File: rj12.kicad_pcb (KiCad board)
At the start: 2 copper layers, 16.3 x 21 mm, 2 parts, among them J1 Conn_01x06, P1 RJ12_Housing

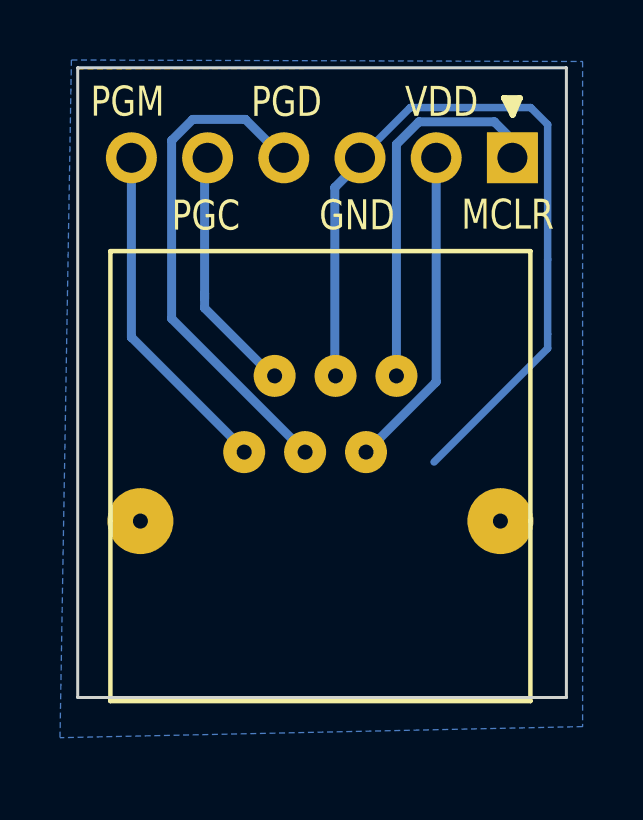
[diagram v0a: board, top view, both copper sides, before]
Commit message: Change the outline more compact
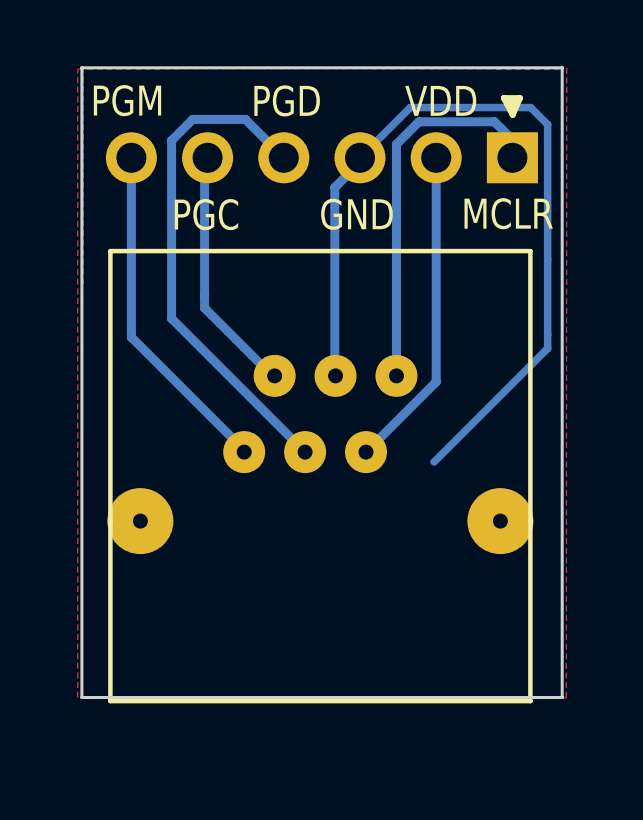
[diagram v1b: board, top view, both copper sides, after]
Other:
- board size 16.3 x 21 mm -> 16 x 21 mm
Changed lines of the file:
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@@
     (links 6)
     (no_connects 0)
-    (area 159.349999 99.449999 175.740001 120.540001)
+    (area 149.500001 95.849945 177.295 121.830001)
     (thickness 1.6)
-    (drawings 31)
+    (drawings 33)
     (tracks 34)
     (zones 0)
@@
     )
   )
+  (dimension 20.98 (width 0.3) (layer Eco1.User)
+    (gr_text "20.980 mm" (at 156 110 270) (layer Eco1.User)
+      (effects (font (size 1.5 1.5) (thickness 0.3)))
+    )
+    (feature1 (pts (xy 159.4 120.49) (xy 154.65 120.49)))
+    (feature2 (pts (xy 159.4 99.51) (xy 154.65 99.51)))
+    (crossbar (pts (xy 157.35 99.51) (xy 157.35 120.49)))
+    (arrow1a (pts (xy 157.35 120.49) (xy 156.763579 119.363496)))
+    (arrow1b (pts (xy 157.35 120.49) (xy 157.936421 119.363496)))
+    (arrow2a (pts (xy 157.35 99.51) (xy 156.763579 100.636504)))
+    (arrow2b (pts (xy 157.35 99.51) (xy 157.936421 100.636504)))
+  )
+  (dimension 16.000012 (width 0.3) (layer Eco1.User)
+    (gr_text "16.000 mm" (at 167.552825 97.239954 359.9283803) (layer Eco1.User)
+      (effects (font (size 1.5 1.5) (thickness 0.3)))
+    )
+    (feature1 (pts (xy 175.55 99.51) (xy 175.554513 95.899955)))
+    (feature2 (pts (xy 159.55 99.49) (xy 159.554513 95.879955)))
+    (crossbar (pts (xy 159.551138 98.579953) (xy 175.551138 98.599953)))
+    (arrow1a (pts (xy 175.551138 98.599953) (xy 174.423902 99.184965)))
+    (arrow1b (pts (xy 175.551138 98.599953) (xy 174.425368 98.012125)))
+    (arrow2a (pts (xy 159.551138 98.579953) (xy 160.676908 99.167781)))
+    (arrow2b (pts (xy 159.551138 98.579953) (xy 160.678374 97.994941)))
+  )
   (gr_line (start 174.14 100.51) (end 173.9 101.07) (layer F.SilkS) (width 0.2))
   (gr_line (start 173.61 100.51) (end 174.14 100.51) (layer F.SilkS) (width 0.2))
-  (gr_line (start 175.69 99.5) (end 175.69 120.49) (layer Edge.Cuts) (width 0.1))
+  (gr_line (start 175.55 99.5) (end 175.55 120.49) (layer Edge.Cuts) (width 0.1))
   (gr_line (start 166.59 116.81) (end 165.91 117.33) (layer B.SilkS) (width 0.2))
   (gr_line (start 166.41 116.54) (end 165.65 116.64) (layer B.SilkS) (width 0.2))
@@
     (effects (font (size 1 1) (thickness 0.25)) (justify mirror))
   )
-  (gr_line (start 159.4 99.5) (end 159.4 120.49) (layer Edge.Cuts) (width 0.1))
-  (gr_line (start 159.4 99.5) (end 175.69 99.5) (layer Edge.Cuts) (width 0.1))
-  (gr_line (start 159.4 120.49) (end 175.69 120.49) (layer Edge.Cuts) (width 0.1))
+  (gr_line (start 159.54 99.5) (end 159.54 120.49) (layer Edge.Cuts) (width 0.1))
+  (gr_line (start 159.54 99.5) (end 175.55 99.5) (layer Edge.Cuts) (width 0.1))
+  (gr_line (start 159.54 120.49) (end 175.55 120.49) (layer Edge.Cuts) (width 0.1))
   (gr_text PGM (at 161.06 100.63) (layer F.SilkS)
     (effects (font (size 1 0.8) (thickness 0.2)))
@@
   (segment (start 171.35 109.97) (end 169.01 112.31) (width 0.3) (layer B.Cu) (net 2))
   (segment (start 171.5 102.5) (end 171.3 102.7) (width 0.3) (layer B.Cu) (net 2))
+  (segment (start 175.065001 105.884999) (end 175.065001 108.374999) (width 0.25) (layer B.Cu) (net 3))
   (segment (start 175.065001 108.854999) (end 171.28 112.64) (width 0.25) (layer B.Cu) (net 3))
   (segment (start 175.065001 108.374999) (end 175.065001 108.854999) (width 0.25) (layer B.Cu) (net 3))
-  (segment (start 175.065001 105.884999) (end 175.065001 108.374999) (width 0.25) (layer B.Cu) (net 3))
+  (segment (start 175.065001 101.389999) (end 175.065001 105.884999) (width 0.25) (layer B.Cu) (net 3))
+  (segment (start 174.499991 100.824989) (end 175.065001 101.389999) (width 0.25) (layer B.Cu) (net 3))
   (segment (start 168.81 102.5) (end 170.485011 100.824989) (width 0.25) (layer B.Cu) (net 3))
   (segment (start 170.485011 100.824989) (end 174.499991 100.824989) (width 0.25) (layer B.Cu) (net 3))
-  (segment (start 174.499991 100.824989) (end 175.065001 101.389999) (width 0.25) (layer B.Cu) (net 3))
-  (segment (start 175.065001 101.389999) (end 175.065001 105.884999) (width 0.25) (layer B.Cu) (net 3))
   (segment (start 168.96 102.5) (end 167.970005 103.489995) (width 0.3) (layer B.Cu) (net 3))
   (segment (start 167.970005 103.489995) (end 167.970005 109.745005) (width 0.3) (layer B.Cu) (net 3))
@@
     (polygon
       (pts
-        (xy 159.19 99.24) (xy 176.23 99.29) (xy 176.23 121.46) (xy 158.81 121.83)
+        (xy 159.58 99.51) (xy 175.53 99.54) (xy 175.55 120.47) (xy 159.54 120.47)
       )
     )

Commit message: Added a txt V.01 to indicate version 1 and added gerber file to be panelized
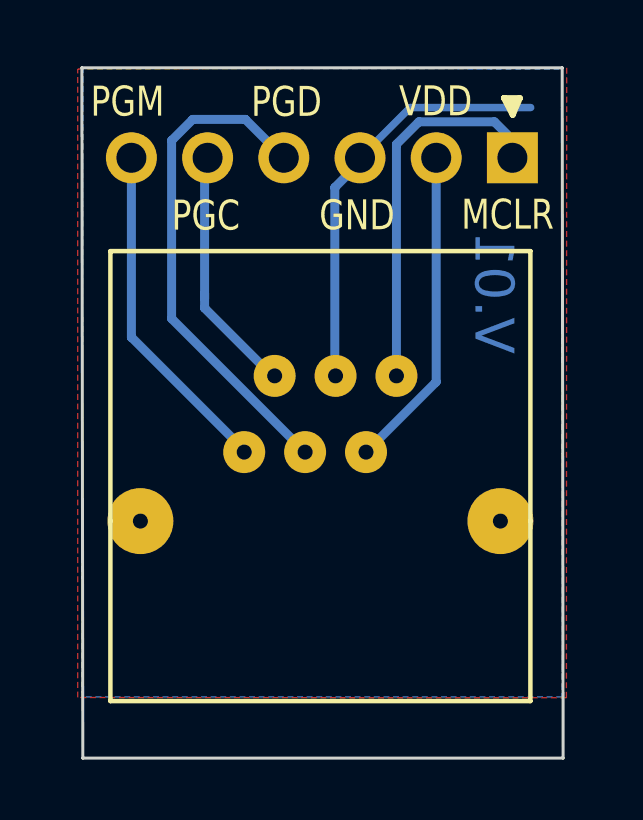
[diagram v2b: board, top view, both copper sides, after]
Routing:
- net pin3: track 27.8 -> 14.1 mm
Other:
- board size 16 x 21 mm -> 16 x 23 mm
- board text added: "V.01"
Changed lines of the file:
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@@
     (links 6)
     (no_connects 0)
-    (area 149.500001 95.849945 177.295 121.830001)
+    (area 150.580402 95.879955 177.295 122.560001)
     (thickness 1.6)
-    (drawings 33)
-    (tracks 34)
+    (drawings 34)
+    (tracks 29)
     (zones 0)
     (modules 2)
@@
     (pad_drill 0.5)
     (pad_to_mask_clearance 0)
-    (aux_axis_origin 0 0)
+    (aux_axis_origin 159.54 99.5)
+    (grid_origin 159.54 99.5)
     (visible_elements 7FFFFFFF)
     (pcbplotparams
-      (layerselection 0x00030_80000001)
-      (usegerberextensions false)
+      (layerselection 0x0ffff_80000001)
+      (usegerberextensions true)
+      (usegerberattributes true)
       (excludeedgelayer true)
       (linewidth 0.100000)
@@
       (viasonmask false)
       (mode 1)
-      (useauxorigin false)
+      (useauxorigin true)
       (hpglpennumber 1)
       (hpglpenspeed 20)
@@
       (psa4output false)
       (plotreference true)
-      (plotvalue true)
+      (plotvalue false)
       (plotinvisibletext false)
       (padsonsilk false)
@@
       (outputformat 1)
       (mirror false)
-      (drillshape 1)
+      (drillshape 0)
       (scaleselection 1)
-      (outputdirectory ""))
+      (outputdirectory RJ-12/))
   )
   (net 0 "")
@@
     )
   )
-  (dimension 20.98 (width 0.3) (layer Eco1.User)
-    (gr_text "20.980 mm" (at 156 110 270) (layer Eco1.User)
+  (dimension 23.000009 (width 0.3) (layer Eco1.User)
+    (gr_text "23.000 mm" (at 157.080401 111.002156 270.0498224) (layer Eco1.User)
       (effects (font (size 1.5 1.5) (thickness 0.3)))
     )
-    (feature1 (pts (xy 159.4 120.49) (xy 154.65 120.49)))
-    (feature2 (pts (xy 159.4 99.51) (xy 154.65 99.51)))
-    (crossbar (pts (xy 157.35 99.51) (xy 157.35 120.49)))
-    (arrow1a (pts (xy 157.35 120.49) (xy 156.763579 119.363496)))
-    (arrow1b (pts (xy 157.35 120.49) (xy 157.936421 119.363496)))
-    (arrow2a (pts (xy 157.35 99.51) (xy 156.763579 100.636504)))
-    (arrow2b (pts (xy 157.35 99.51) (xy 157.936421 100.636504)))
+    (feature1 (pts (xy 159.57 122.5) (xy 155.740402 122.50333)))
+    (feature2 (pts (xy 159.55 99.5) (xy 155.720402 99.50333)))
+    (crossbar (pts (xy 158.420401 99.500982) (xy 158.440401 122.500982)))
+    (arrow1a (pts (xy 158.440401 122.500982) (xy 157.853001 121.374989)))
+    (arrow1b (pts (xy 158.440401 122.500982) (xy 159.025842 121.373969)))
+    (arrow2a (pts (xy 158.420401 99.500982) (xy 157.83496 100.627995)))
+    (arrow2b (pts (xy 158.420401 99.500982) (xy 159.007801 100.626975)))
+  )
+  (gr_text V.01 (at 173.26 107.01 270) (layer B.Cu)
+    (effects (font (size 1.3 1.3) (thickness 0.3)) (justify mirror))
   )
   (dimension 16.000012 (width 0.3) (layer Eco1.User)
@@
   (gr_line (start 174.14 100.51) (end 173.9 101.07) (layer F.SilkS) (width 0.2))
   (gr_line (start 173.61 100.51) (end 174.14 100.51) (layer F.SilkS) (width 0.2))
-  (gr_line (start 175.55 99.5) (end 175.55 120.49) (layer Edge.Cuts) (width 0.1))
+  (gr_line (start 175.55 99.5) (end 175.58 122.51) (layer Edge.Cuts) (width 0.1))
   (gr_line (start 166.59 116.81) (end 165.91 117.33) (layer B.SilkS) (width 0.2))
   (gr_line (start 166.41 116.54) (end 165.65 116.64) (layer B.SilkS) (width 0.2))
@@
     (effects (font (size 1 1) (thickness 0.25)) (justify mirror))
   )
-  (gr_line (start 159.54 99.5) (end 159.54 120.49) (layer Edge.Cuts) (width 0.1))
+  (gr_line (start 159.54 99.5) (end 159.57 122.51) (layer Edge.Cuts) (width 0.1))
   (gr_line (start 159.54 99.5) (end 175.55 99.5) (layer Edge.Cuts) (width 0.1))
-  (gr_line (start 159.54 120.49) (end 175.55 120.49) (layer Edge.Cuts) (width 0.1))
+  (gr_line (start 159.57 122.51) (end 175.58 122.51) (layer Edge.Cuts) (width 0.1))
   (gr_text PGM (at 161.06 100.63) (layer F.SilkS)
     (effects (font (size 1 0.8) (thickness 0.2)))
@@
     (effects (font (size 1 0.8) (thickness 0.2)))
   )
-  (gr_text VDD (at 171.53 100.64) (layer F.SilkS)
+  (gr_text VDD (at 171.33 100.62) (layer F.SilkS)
     (effects (font (size 1 0.8) (thickness 0.2)))
   )
@@
   (segment (start 171.35 109.97) (end 169.01 112.31) (width 0.3) (layer B.Cu) (net 2))
   (segment (start 171.5 102.5) (end 171.3 102.7) (width 0.3) (layer B.Cu) (net 2))
-  (segment (start 175.065001 105.884999) (end 175.065001 108.374999) (width 0.25) (layer B.Cu) (net 3))
-  (segment (start 175.065001 108.854999) (end 171.28 112.64) (width 0.25) (layer B.Cu) (net 3))
-  (segment (start 175.065001 108.374999) (end 175.065001 108.854999) (width 0.25) (layer B.Cu) (net 3))
-  (segment (start 175.065001 101.389999) (end 175.065001 105.884999) (width 0.25) (layer B.Cu) (net 3))
-  (segment (start 174.499991 100.824989) (end 175.065001 101.389999) (width 0.25) (layer B.Cu) (net 3))
   (segment (start 168.81 102.5) (end 170.485011 100.824989) (width 0.25) (layer B.Cu) (net 3))
   (segment (start 170.485011 100.824989) (end 174.499991 100.824989) (width 0.25) (layer B.Cu) (net 3))
